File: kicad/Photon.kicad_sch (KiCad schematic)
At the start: 1 part

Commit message: kicad update, finalizing
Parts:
- added J6, J7: Conn_01x19_Pin, Connector_PinHeader_2.54mm:PinHeader_1x19_P2.54mm_Vertical, symbol Connector:Conn_01x19_Pin
- added J8, J9: Conn_01x19_Pin, symbol Connector:Conn_01x15_Pin
- added U8: ~, symbol JP_Library:ESP32_DEVKIT_V1_DOIT
- PHOTON2: footprint (none) -> JP_Library:MODULE_ESP32-DEVKITC-32U; symbol New_Library:Photon2 -> JP_Library:ESP32-DEVKITC-32U; Availability (none) -> In Stock; Check_prices (none) -> https://www.snapeda.com/parts/ESP32-DEVKITC-32U/Espressif+S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; MANUFACTURER (none) -> ESPRESSIF; MF (none) -> Espressif Systems; MP (none) -> ESP32-DEVKITC-32U; PARTREV (none) -> N/A; Package (none) -> CUSTOM-38 ESPRESSIF; Price (none) -> None; Purchase-URL (none) -> https://www.snapeda.com/api/url_track_click_mouser/?unipart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; STANDARD (none) -> Manufacturer Recommendations; SnapEDA_Link (none) -> https://www.snapeda.com/parts/ESP32-DEVKITC-32U/Espressif+S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
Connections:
- net UART_RX: no longer PHOTON2.TX
- net UART_TX: no longer PHOTON2.RX
- removed net +3V3: PHOTON2.3V3
- removed net GND: PHOTON2.GND
- new net: J8.1 (Pin_1), U8.1 (3V3)
- new net: J8.10 (Pin_10), U8.10 (D19)
- new net: J8.11 (Pin_11), U8.11 (D21)
- new net: J8.12 (Pin_12), U8.12 (RX0)
- new net: J8.13 (Pin_13), U8.13 (TX0)
- new net: J8.2 (Pin_2), U8.2 (GND)
- new net: J8.14 (Pin_14), U8.26 (D14)
- new net: J8.3 (Pin_3), U8.3 (D15)
- new net: J8.4 (Pin_4), U8.4 (D2)
- new net: J8.5 (Pin_5), U8.5 (D4)
- new net: J8.6 (Pin_6), U8.6 (RX2)
- new net: J8.7 (Pin_7), U8.7 (TX2)
- new net: J8.8 (Pin_8), U8.8 (D5)
- new net: J8.9 (Pin_9), U8.9 (D18)
- new net: J7.1 (Pin_1), PHOTON2.1 (3V3)
- new net: J7.10 (Pin_10), PHOTON2.10 (IO26)
- new net: J7.11 (Pin_11), PHOTON2.11 (IO27)
- new net: J7.12 (Pin_12), PHOTON2.12 (IO14)
- new net: J7.13 (Pin_13), PHOTON2.13 (IO12)
- new net: J7.14 (Pin_14), PHOTON2.14 (GND1)
- new net: J7.15 (Pin_15), PHOTON2.15 (IO13)
- new net: J7.16 (Pin_16), PHOTON2.16 (SD2)
- new net: J7.17 (Pin_17), PHOTON2.17 (SD3)
- new net: J7.18 (Pin_18), PHOTON2.18 (CMD)
- new net: J7.19 (Pin_19), PHOTON2.19 (EXT_5V)
- new net: J7.2 (Pin_2), PHOTON2.2 (EN)
- new net: J6.19 (Pin_19), PHOTON2.20 (CLK)
- new net: J6.18 (Pin_18), PHOTON2.21 (SD0)
- new net: J6.17 (Pin_17), PHOTON2.22 (SD1)
- new net: J6.16 (Pin_16), PHOTON2.23 (IO15)
- new net: J6.15 (Pin_15), PHOTON2.24 (IO2)
- new net: J6.14 (Pin_14), PHOTON2.25 (IO0)
- new net: J6.13 (Pin_13), PHOTON2.26 (IO4)
- new net: J6.12 (Pin_12), PHOTON2.27 (IO16)
- new net: J6.11 (Pin_11), PHOTON2.28 (IO17)
- new net: J6.10 (Pin_10), PHOTON2.29 (IO5)
- new net: J7.3 (Pin_3), PHOTON2.3 (SENSOR_VP)
- new net: J6.9 (Pin_9), PHOTON2.30 (IO18)
- new net: J6.8 (Pin_8), PHOTON2.31 (IO19)
- new net: J6.7 (Pin_7), PHOTON2.32 (GND2)
- new net: J6.6 (Pin_6), PHOTON2.33 (IO21)
- new net: J6.5 (Pin_5), PHOTON2.34 (RXD0)
- new net: J6.4 (Pin_4), PHOTON2.35 (TXD0)
- new net: J6.3 (Pin_3), PHOTON2.36 (IO22)
- new net: J6.2 (Pin_2), PHOTON2.37 (IO23)
- new net: J6.1 (Pin_1), PHOTON2.38 (GND3)
- new net: J7.4 (Pin_4), PHOTON2.4 (SENSOR_VN)
- new net: J7.5 (Pin_5), PHOTON2.5 (IO34)
- new net: J7.6 (Pin_6), PHOTON2.6 (IO35)
- new net: J7.7 (Pin_7), PHOTON2.7 (IO32)
- new net: J7.8 (Pin_8), PHOTON2.8 (IO33)
- new net: J7.9 (Pin_9), PHOTON2.9 (IO25)

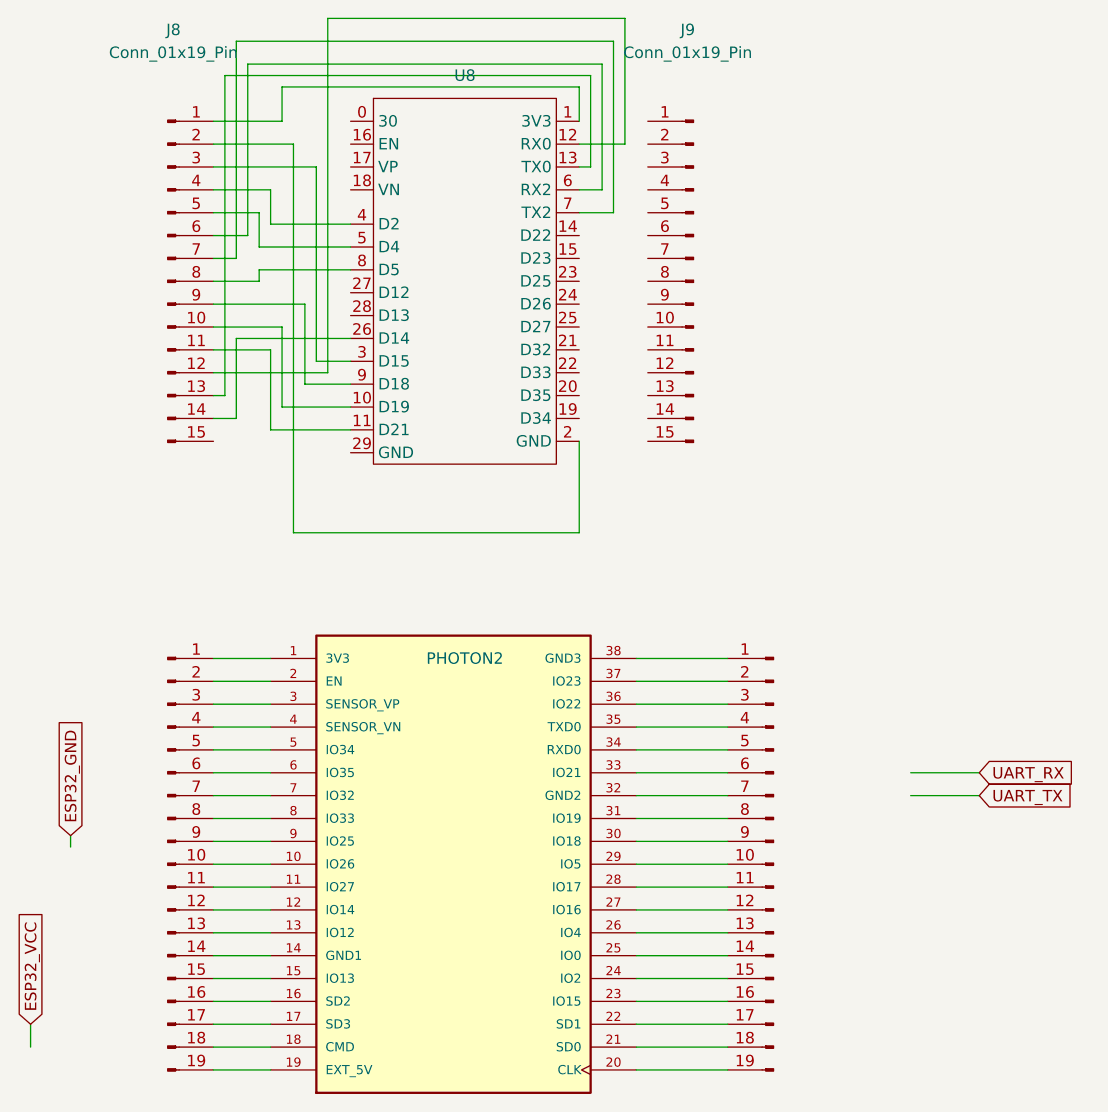
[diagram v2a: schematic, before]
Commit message: switch to SPIs
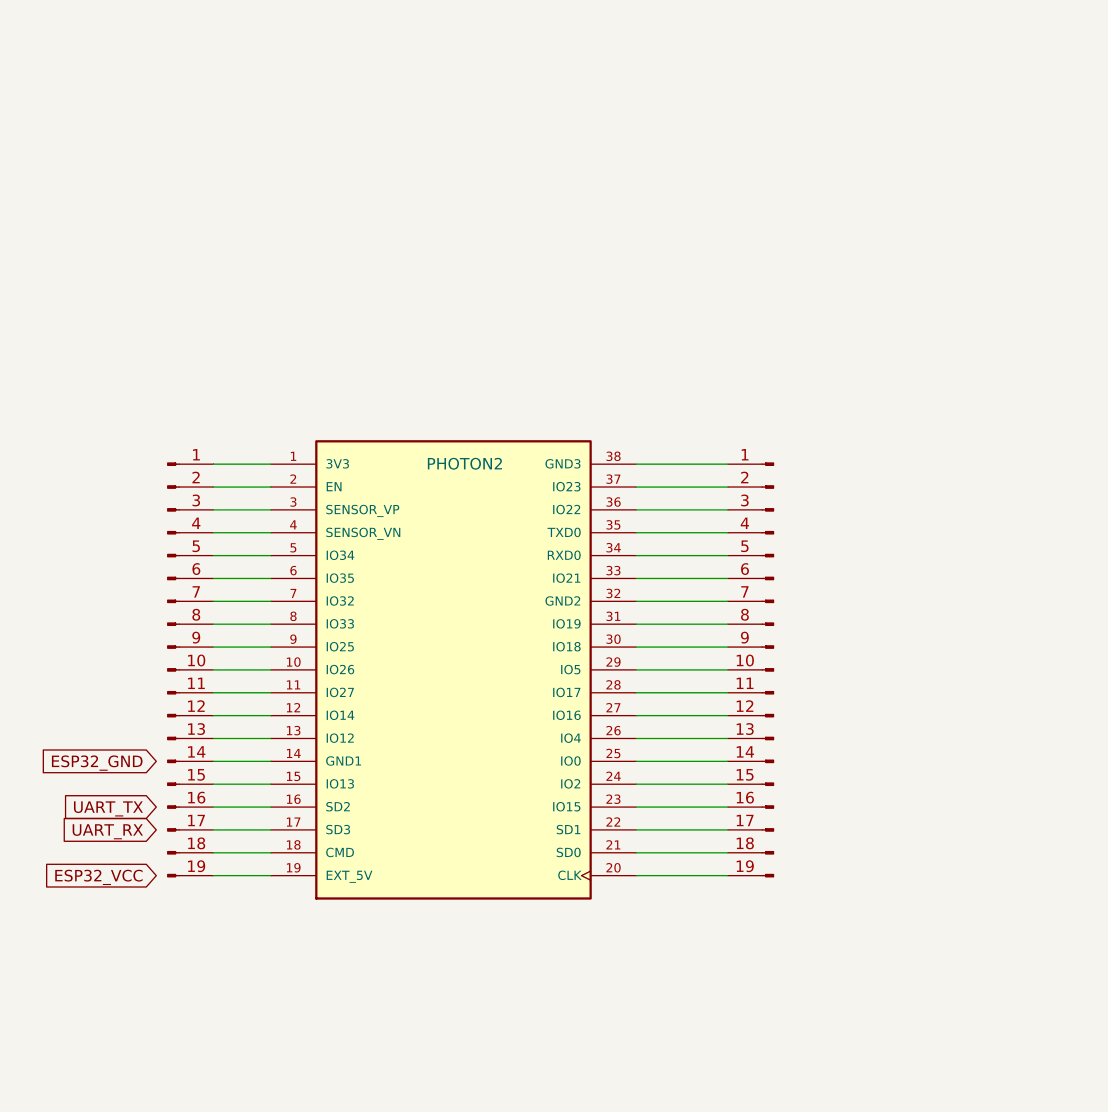
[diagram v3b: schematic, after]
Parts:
- removed J8, J9: Conn_01x19_Pin, symbol Connector:Conn_01x15_Pin
- removed U8: ~, symbol JP_Library:ESP32_DEVKIT_V1_DOIT
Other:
- moved on the sheet: PHOTON2
